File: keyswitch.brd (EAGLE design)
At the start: 235.4 x 78.3 mm, 45 parts

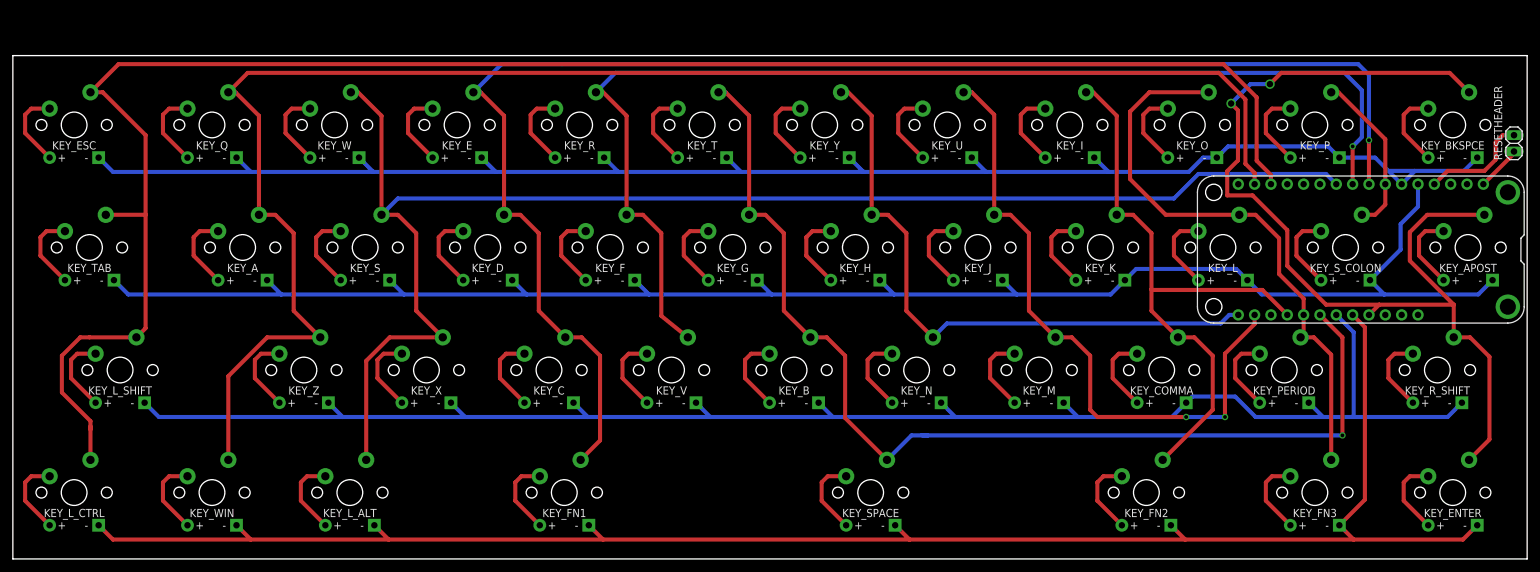
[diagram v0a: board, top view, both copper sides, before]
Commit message: modified to remove vias
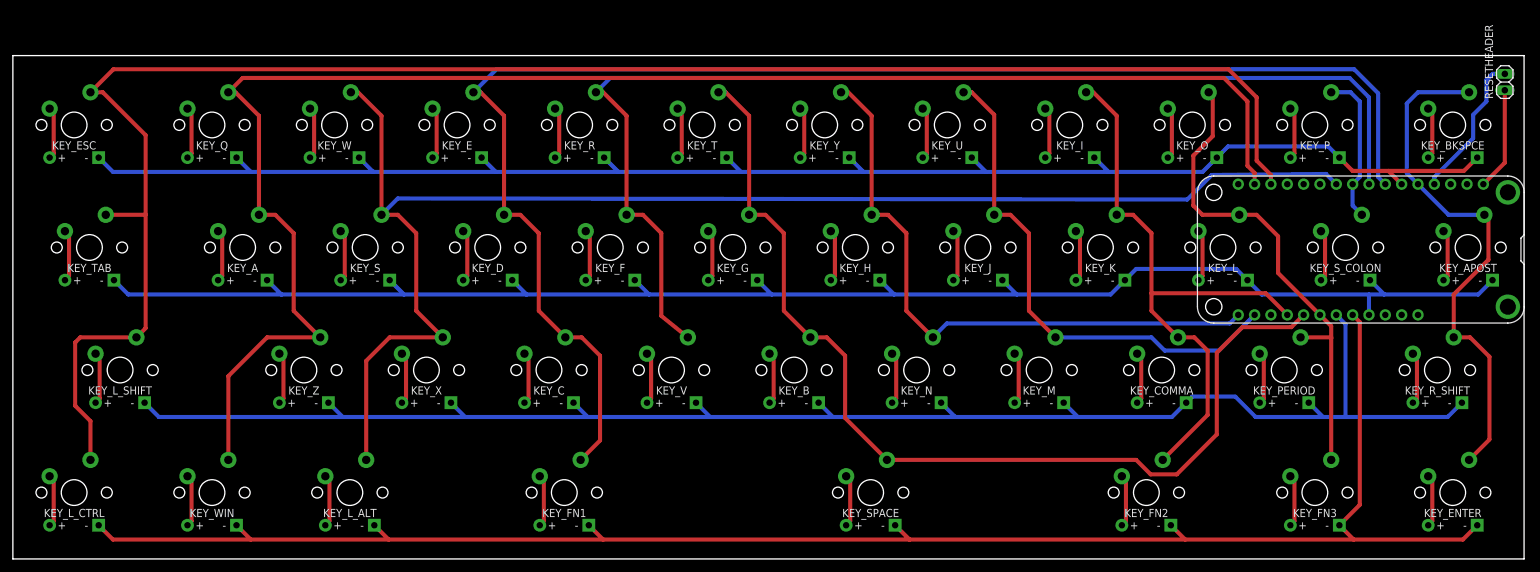
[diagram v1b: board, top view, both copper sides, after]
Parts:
- moved RESETHEADER 9.63 mm to (222.4, 6.67)
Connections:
- net N$35: now also FEATHER.7; no longer FEATHER.8
- net N$46: now also FEATHER.21; no longer FEATHER.22
- net N$49: now also FEATHER.8; no longer FEATHER.9
- net N$52: now also FEATHER.22; no longer FEATHER.21
- net N$55: now also FEATHER.9; no longer FEATHER.7
- net N$56: now also FEATHER.5; no longer FEATHER.25
- net N$72: now also FEATHER.25; no longer FEATHER.5
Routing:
- net N$56: track 159.4 -> 81.7 mm, vias 2 -> 0
- net N$54: track 100.4 -> 80.4 mm, vias 2 -> 0
- net N$72: track 262.6 -> 247.8 mm
- net N$52: track 90.3 -> 77.4 mm
- net N$46: track 165.1 -> 155.0 mm, vias 1 -> 0
- net N$40: track 7.05 -> 16.0 mm
- net GND: track 17.1 -> 22.8 mm
- net N$10: track 12.5 -> 8.15 mm
- net N$23: track 12.5 -> 8.15 mm
- net N$20: track 12.5 -> 8.15 mm
- net N$36: track 12.5 -> 8.15 mm
- net N$34: track 12.5 -> 8.15 mm
- net N$32: track 12.5 -> 8.15 mm
- net N$7: track 12.5 -> 8.15 mm
- net N$6: track 12.5 -> 8.15 mm
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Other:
- board size 235.4 x 78.3 mm -> 234.9 x 78.3 mm
